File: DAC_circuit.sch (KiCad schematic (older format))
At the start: 22 parts, among them U17 SN65LVDS1DBV, U24 AD9747BCPZ

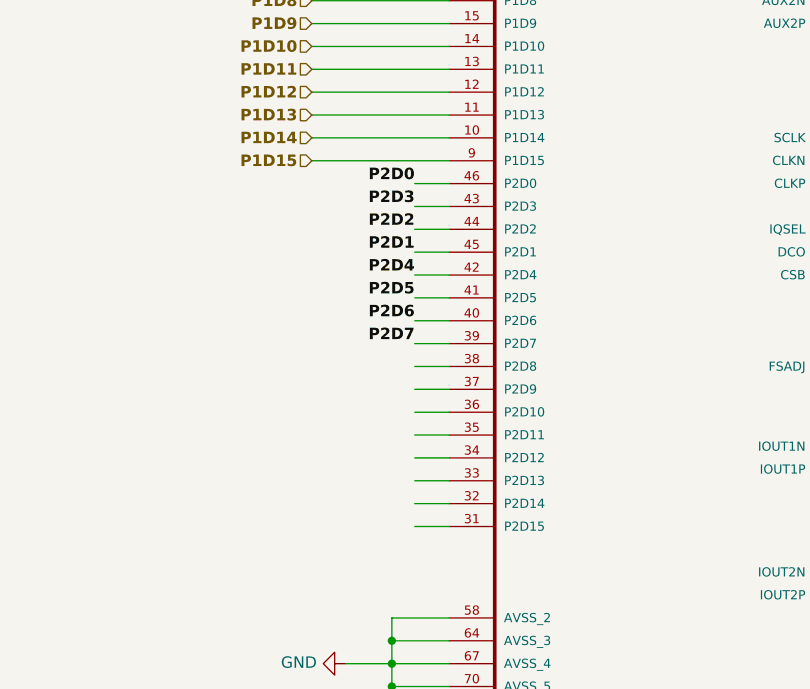
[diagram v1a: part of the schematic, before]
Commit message: Layout done for ADC + LVDS and DAC -> FPGA
Signed-off-by: Alexis Jeandet <alexis.jeandet@member.fsf.org>
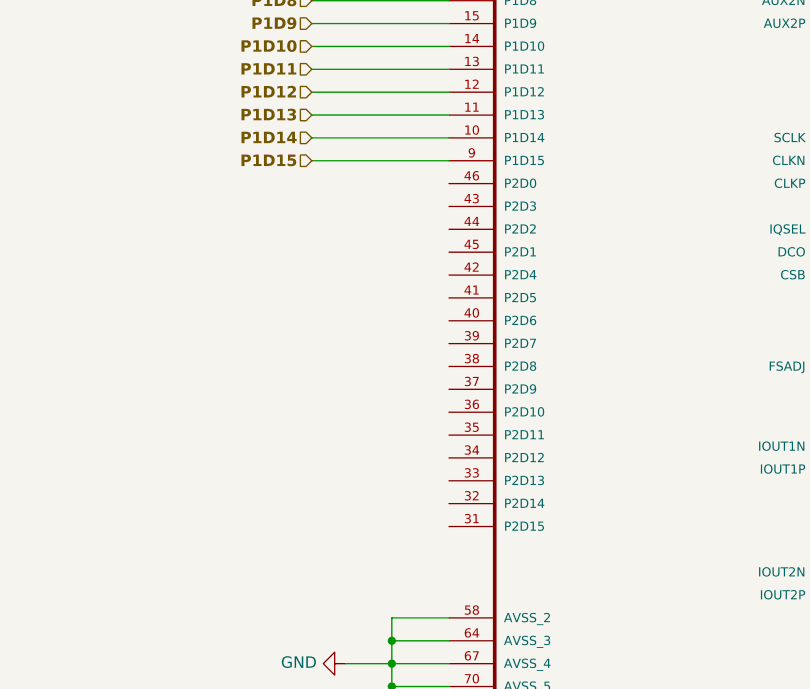
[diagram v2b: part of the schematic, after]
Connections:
- net labels removed: P2D0, P2D1, P2D2, P2D3, P2D4, P2D5, P2D6, P2D7
- wire segments 167 -> 151

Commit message: Added #3.3V and #1.2V supply, completed ADC to USB board layout, added DAC FPGA to USB board bus.
Signed-off-by: Alexis Jeandet <alexis.jeandet@member.fsf.org>
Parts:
- renumbered C1 to C1001, C2 to C1002, C3 to C1003, C4 to C1004, C6 to C1005, C5 to C1006, C7 to C1007, C8 to C1008, C9 to C1009, C10 to C1010, C11 to C1011, C12 to C1012, C15 to C1013, C17 to C1014, C14 to C1015, R1 to R1001, R2 to R1002, R3 to R1003, R37 to R1004, R5 to R1005, U24 to U1001, U17 to U1002

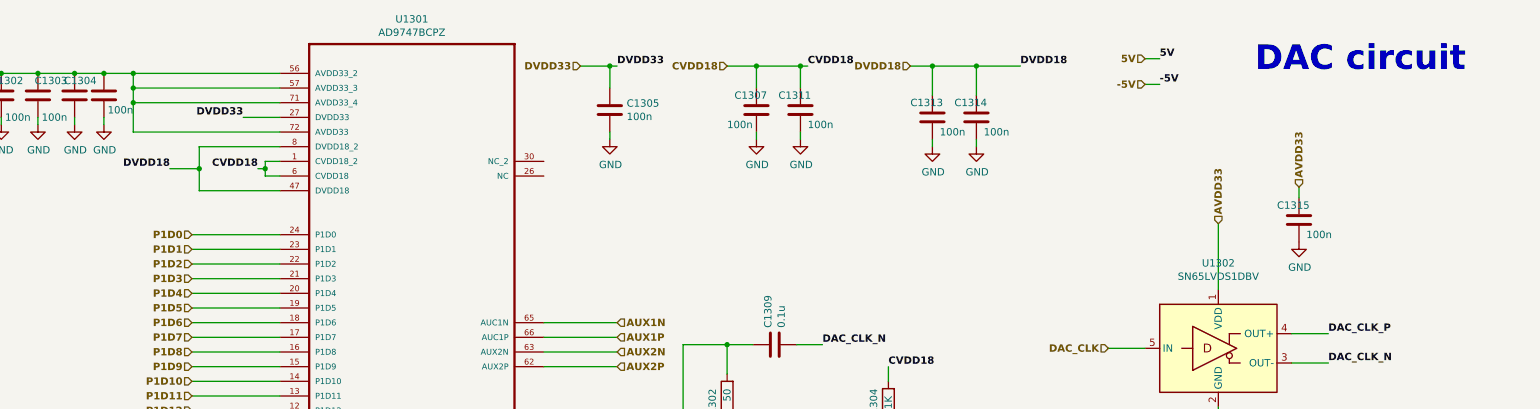
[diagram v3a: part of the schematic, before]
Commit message: Layout complete, needs silk screen cleanup and few checks
Signed-off-by: Alexis Jeandet <alexis.jeandet@member.fsf.org>
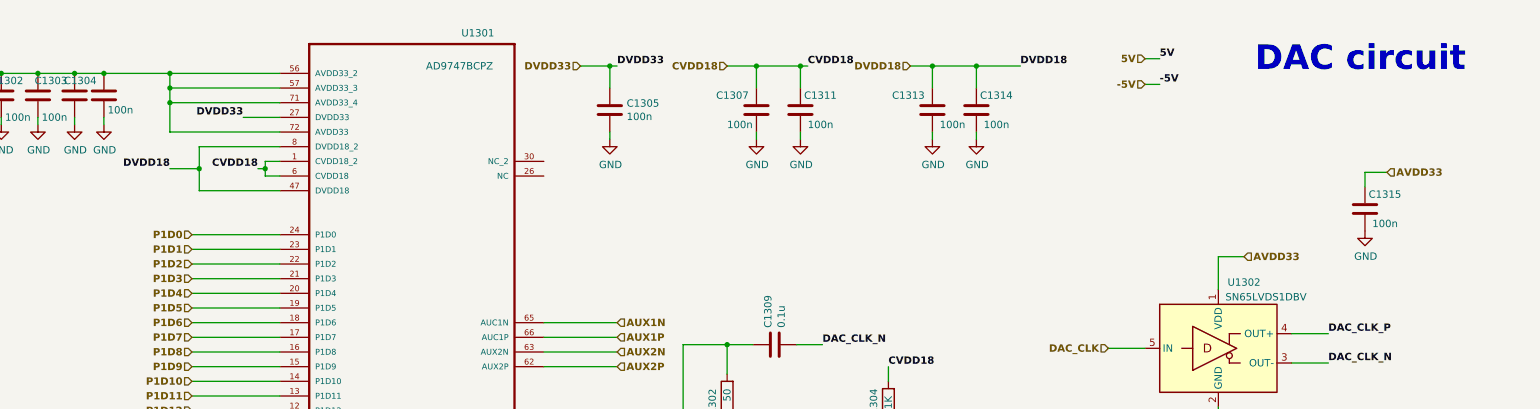
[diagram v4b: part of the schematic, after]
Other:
- moved on the sheet: C1313, C1314, C1315
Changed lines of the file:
@@
 Connection ~ 2750 6450
 Connection ~ 2450 1500
-Connection ~ 2000 1050
+Connection ~ 2250 1050
 Connection ~ 5250 800
-Connection ~ 2000 950
+Connection ~ 2250 950
 Connection ~ 1100 850
 Connection ~ 1350 850
 Connection ~ 1600 850
 Connection ~ 1800 850
-Connection ~ 2000 850
+Connection ~ 2250 850
 Connection ~ 6250 800
 Connection ~ 6550 800
@@
 	1600 1200 1600 1150
 Wire Wire Line
-	1800 850  2000 850
+	1800 850  2250 850
 Wire Wire Line
 	1800 1150 1800 1200
 Wire Wire Line
-	2000 850  2000 950
+	2250 850  2250 950
 Wire Wire Line
-	2000 850  3000 850
+	2250 850  3000 850
 Wire Wire Line
-	2000 950  2000 1050
+	2250 950  2250 1050
 Wire Wire Line
-	2000 1050 2000 1250
+	2250 1050 2250 1250
 Wire Wire Line
-	2000 1050 3000 1050
+	2250 1050 3000 1050
 Wire Wire Line
-	2000 1250 3000 1250
+	2250 1250 3000 1250
 Wire Wire Line
 	2250 1500 2450 1500
@@
 	2900 1500 2900 1550
 Wire Wire Line
-	3000 950  2000 950
+	3000 950  2250 950
 Wire Wire Line
 	3000 1150 2750 1150
@@
 	7450 800  7750 800
 Wire Wire Line
-	7450 1000 7450 800
+	7450 950  7450 800
 Wire Wire Line
-	7450 1300 7450 1350
+	7450 1250 7450 1300
 Wire Wire Line
 	7150 2850 7150 2950
@@
 	7750 800  8050 800
 Wire Wire Line
-	7750 1000 7750 800
+	7750 950  7750 800
 Wire Wire Line
-	7750 1300 7750 1350
+	7750 1250 7750 1300
 Wire Wire Line
 	8900 750  9000 750
@@
 	8900 2725 8650 2725
 Wire Wire Line
-	9400 1875 9400 2325
+	9400 2100 9400 2325
 Wire Wire Line
 	9400 3125 9400 3225
@@
 Wire Wire Line
 	9900 2825 10150 2825
-Wire Wire Line
-	9950 1700 9950 1625
 Text Notes 9650 850  0    168  ~ 34
 DAC circuit
@@
 Text HLabel 8650 2725 0    50   Input ~ 10
 DAC_CLK
-Text HLabel 9400 1875 1    50   Input ~ 10
+Text HLabel 9575 2100 2    50   Input ~ 10
 AVDD33
-Text HLabel 9950 1625 1    50   Input ~ 10
+Text HLabel 10550 1525 2    50   Input ~ 10
 AVDD33
 $Comp
@@
 L power:GND #PWR?
 U 1 1 5CA9778D
-P 7450 1350
+P 7450 1300
 AR Path="/5C89FEE5/5CA5C1C3/5CA9778D" Ref="#PWR?"  Part="1"
 AR Path="/5C89FEE5/5CA33249/5CA9778D" Ref="#PWR?"  Part="1"
@@
 AR Path="/5F420A26/5F604603/5CA9778D" Ref="#PWR01315"  Part="1"
 AR Path="/5F420A26/5FC968EA/5CA9778D" Ref="#PWR?"  Part="1"
-F 0 "#PWR01315" H 7450 1100 50  0001 C CNN
-F 1 "GND" H 7455 1177 50  0000 C CNN
-F 2 "" H 7450 1350 50  0001 C CNN
-F 3 "" H 7450 1350 50  0001 C CNN
-	1    7450 1350
+F 0 "#PWR01315" H 7450 1050 50  0001 C CNN
+F 1 "GND" H 7455 1127 50  0000 C CNN
+F 2 "" H 7450 1300 50  0001 C CNN
+F 3 "" H 7450 1300 50  0001 C CNN
+	1    7450 1300
 	1    0    0    -1
 $EndComp
@@
 L power:GND #PWR?
 U 1 1 5CBBD4FE
-P 7750 1350
+P 7750 1300
 AR Path="/5C89FEE5/5CA5C1C3/5CBBD4FE" Ref="#PWR?"  Part="1"
 AR Path="/5C89FEE5/5CA33249/5CBBD4FE" Ref="#PWR?"  Part="1"
@@
 AR Path="/5F420A26/5F604603/5CBBD4FE" Ref="#PWR01316"  Part="1"
 AR Path="/5F420A26/5FC968EA/5CBBD4FE" Ref="#PWR?"  Part="1"
-F 0 "#PWR01316" H 7750 1100 50  0001 C CNN
-F 1 "GND" H 7755 1177 50  0000 C CNN
-F 2 "" H 7750 1350 50  0001 C CNN
-F 3 "" H 7750 1350 50  0001 C CNN
-	1    7750 1350
+F 0 "#PWR01316" H 7750 1050 50  0001 C CNN
+F 1 "GND" H 7755 1127 50  0000 C CNN
+F 2 "" H 7750 1300 50  0001 C CNN
+F 3 "" H 7750 1300 50  0001 C CNN
+	1    7750 1300
 	1    0    0    -1
 $EndComp
@@
 L power:GND #PWR?
 U 1 1 5DF0A06F
-P 9950 2000
+P 10400 1925
 AR Path="/5C89FEE5/5CA5C1C3/5DF0A06F" Ref="#PWR?"  Part="1"
 AR Path="/5C89FEE5/5CA33249/5DF0A06F" Ref="#PWR?"  Part="1"
@@
 AR Path="/5F420A26/5F604603/5DF0A06F" Ref="#PWR01318"  Part="1"
 AR Path="/5F420A26/5FC968EA/5DF0A06F" Ref="#PWR?"  Part="1"
-F 0 "#PWR01318" H 9950 1750 50  0001 C CNN
-F 1 "GND" H 9955 1827 50  0000 C CNN
-F 2 "" H 9950 2000 50  0001 C CNN
-F 3 "" H 9950 2000 50  0001 C CNN
-	1    9950 2000
+F 0 "#PWR01318" H 10400 1675 50  0001 C CNN
+F 1 "GND" H 10405 1752 50  0000 C CNN
+F 2 "" H 10400 1925 50  0001 C CNN
+F 3 "" H 10400 1925 50  0001 C CNN
+	1    10400 1925
 	1    0    0    -1
 $EndComp
@@
 AR Path="/5F420A26/5F604603/5CBDCF09" Ref="C1307"  Part="1"
 AR Path="/5F420A26/5FC968EA/5CBDCF09" Ref="C?"  Part="1"
-F 0 "C1307" H 6100 1200 50  0000 L CNN
+F 0 "C1307" H 5975 1200 50  0000 L CNN
 F 1 "100n" H 6050 1000 50  0000 L CNN
 F 2 "Capacitor_SMD:C_0603_1608Metric" H 6288 950 50  0001 C CNN
@@
 AR Path="/5F420A26/5F604603/5CBEEAFB" Ref="C1311"  Part="1"
 AR Path="/5F420A26/5FC968EA/5CBEEAFB" Ref="C?"  Part="1"
-F 0 "C1311" H 6400 1200 50  0000 L CNN
+F 0 "C1311" H 6575 1200 50  0000 L CNN
 F 1 "100n" H 6600 1000 50  0000 L CNN
 F 2 "Capacitor_SMD:C_0603_1608Metric" H 6588 950 50  0001 C CNN
@@
 L Device:C C?
 U 1 1 5CA97787
-P 7450 1150
+P 7450 1100
 AR Path="/5CEC3473/5CEC474F/5CA97787" Ref="C?"  Part="1"
 AR Path="/5CF60054/5CEC474F/5CA97787" Ref="C?"  Part="1"
@@
 AR Path="/5F420A26/5F604603/5CA97787" Ref="C1313"  Part="1"
 AR Path="/5F420A26/5FC968EA/5CA97787" Ref="C?"  Part="1"
-F 0 "C1313" H 7300 1250 50  0000 L CNN
-F 1 "100n" H 7500 1050 50  0000 L CNN
-F 2 "Capacitor_SMD:C_0603_1608Metric" H 7488 1000 50  0001 C CNN
-F 3 "~" H 7450 1150 50  0001 C CNN
-	1    7450 1150
+F 0 "C1313" H 7175 1200 50  0000 L CNN
+F 1 "100n" H 7500 1000 50  0000 L CNN
+F 2 "Capacitor_SMD:C_0603_1608Metric" H 7488 950 50  0001 C CNN
+F 3 "~" H 7450 1100 50  0001 C CNN
+	1    7450 1100
 	1    0    0    -1
 $EndComp
@@
 L Device:C C?
 U 1 1 5CBBD504
-P 7750 1150
+P 7750 1100
 AR Path="/5CEC3473/5CEC474F/5CBBD504" Ref="C?"  Part="1"
 AR Path="/5CF60054/5CEC474F/5CBBD504" Ref="C?"  Part="1"
@@
 AR Path="/5F420A26/5F604603/5CBBD504" Ref="C1314"  Part="1"
 AR Path="/5F420A26/5FC968EA/5CBBD504" Ref="C?"  Part="1"
-F 0 "C1314" H 7600 1250 50  0000 L CNN
-F 1 "100n" H 7800 1050 50  0000 L CNN
-F 2 "Capacitor_SMD:C_0603_1608Metric" H 7788 1000 50  0001 C CNN
-F 3 "~" H 7750 1150 50  0001 C CNN
-	1    7750 1150
+F 0 "C1314" H 7775 1200 50  0000 L CNN
+F 1 "100n" H 7800 1000 50  0000 L CNN
+F 2 "Capacitor_SMD:C_0603_1608Metric" H 7788 950 50  0001 C CNN
+F 3 "~" H 7750 1100 50  0001 C CNN
+	1    7750 1100
 	1    0    0    -1
 $EndComp
@@
 L Device:C C?
 U 1 1 5DECBC16
-P 9950 1850
+P 10400 1775
 AR Path="/5CEC3473/5CEC474F/5DECBC16" Ref="C?"  Part="1"
 AR Path="/5CF60054/5CEC474F/5DECBC16" Ref="C?"  Part="1"
@@
 AR Path="/5F420A26/5F604603/5DECBC16" Ref="C1315"  Part="1"
 AR Path="/5F420A26/5FC968EA/5DECBC16" Ref="C?"  Part="1"
-F 0 "C1315" H 9800 1950 50  0000 L CNN
-F 1 "100n" H 10000 1750 50  0000 L CNN
-F 2 "Capacitor_SMD:C_0603_1608Metric" H 9988 1700 50  0001 C CNN
-F 3 "~" H 9950 1850 50  0001 C CNN
-	1    9950 1850
+F 0 "C1315" H 10425 1875 50  0000 L CNN
+F 1 "100n" H 10450 1675 50  0000 L CNN
+F 2 "Capacitor_SMD:C_0603_1608Metric" H 10438 1625 50  0001 C CNN
+F 3 "~" H 10400 1775 50  0001 C CNN
+	1    10400 1775
 	1    0    0    -1
 $EndComp
@@
 AR Path="/5F420A26/5F604603/5E0B5B61" Ref="U1302"  Part="1"
 AR Path="/5F420A26/5FC968EA/5E0B5B61" Ref="U?"  Part="1"
-F 0 "U1302" H 9400 3306 50  0000 C CNN
-F 1 "SN65LVDS1DBV" H 9400 3215 50  0000 C CNN
+F 0 "U1302" H 9575 3175 50  0000 C CNN
+F 1 "SN65LVDS1DBV" H 9725 3075 50  0000 C CNN
 F 2 "Package_TO_SOT_SMD:SOT-23-5" H 9400 2275 50  0001 C CNN
 F 3 "http://www.ti.com/lit/ds/symlink/sn65lvds1.pdf" H 9400 2825 50  0001 C CNN
@@
 AR Path="/5F420A26/5F604603/5CA5B6E2" Ref="U1301"  Part="1"
 AR Path="/5F420A26/5FC968EA/5CA5B6E2" Ref="U?"  Part="1"
-F 0 "U1301" H 3900 6820 50  0000 C CNN
-F 1 "AD9747BCPZ" H 3900 6729 50  0000 C CNN
+F 0 "U1301" H 4350 6725 50  0000 C CNN
+F 1 "AD9747BCPZ" H 4225 6500 50  0000 C CNN
 F 2 "Package_CSP:LFCSP-72-1EP_10x10mm_P0.5mm_EP5.3x5.3mm_ThermalVias" H 3900 3650 50  0001 L BNN
 F 3 "" H 3900 3650 50  0001 L BNN
@@
 Wire Wire Line
 	6500 5625 6300 5625
+Wire Wire Line
+	10550 1525 10400 1525
+Wire Wire Line
+	10400 1525 10400 1625
+Wire Wire Line
+	9575 2100 9400 2100
 $EndSCHEMATC
